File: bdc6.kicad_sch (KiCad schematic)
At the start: 0 parts

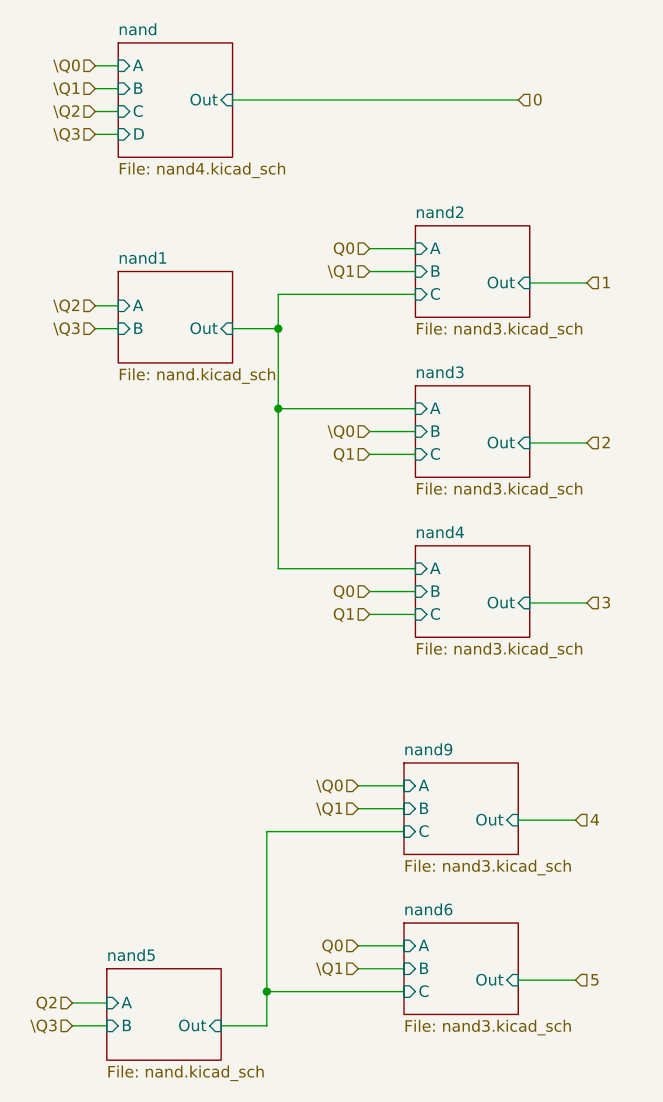
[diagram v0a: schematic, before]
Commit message: corrected output/input type of pins
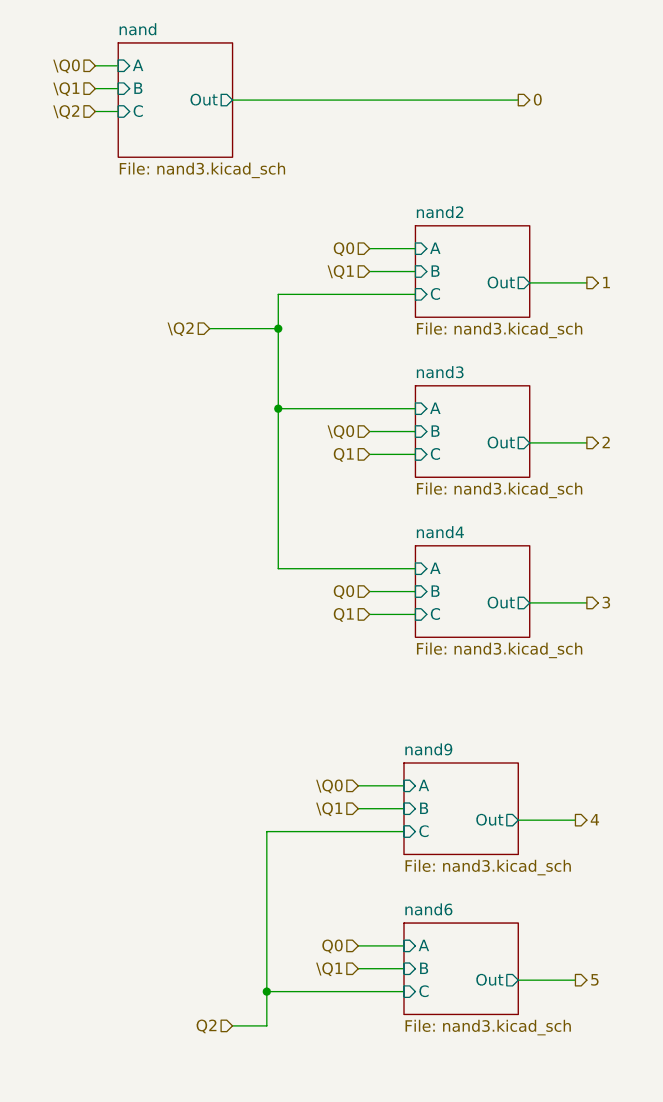
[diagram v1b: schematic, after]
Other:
- removed sheet nand1
- removed sheet nand5
- sheet nand: file nand4.kicad_sch -> nand3.kicad_sch
- sheet nand ports: added none; removed D

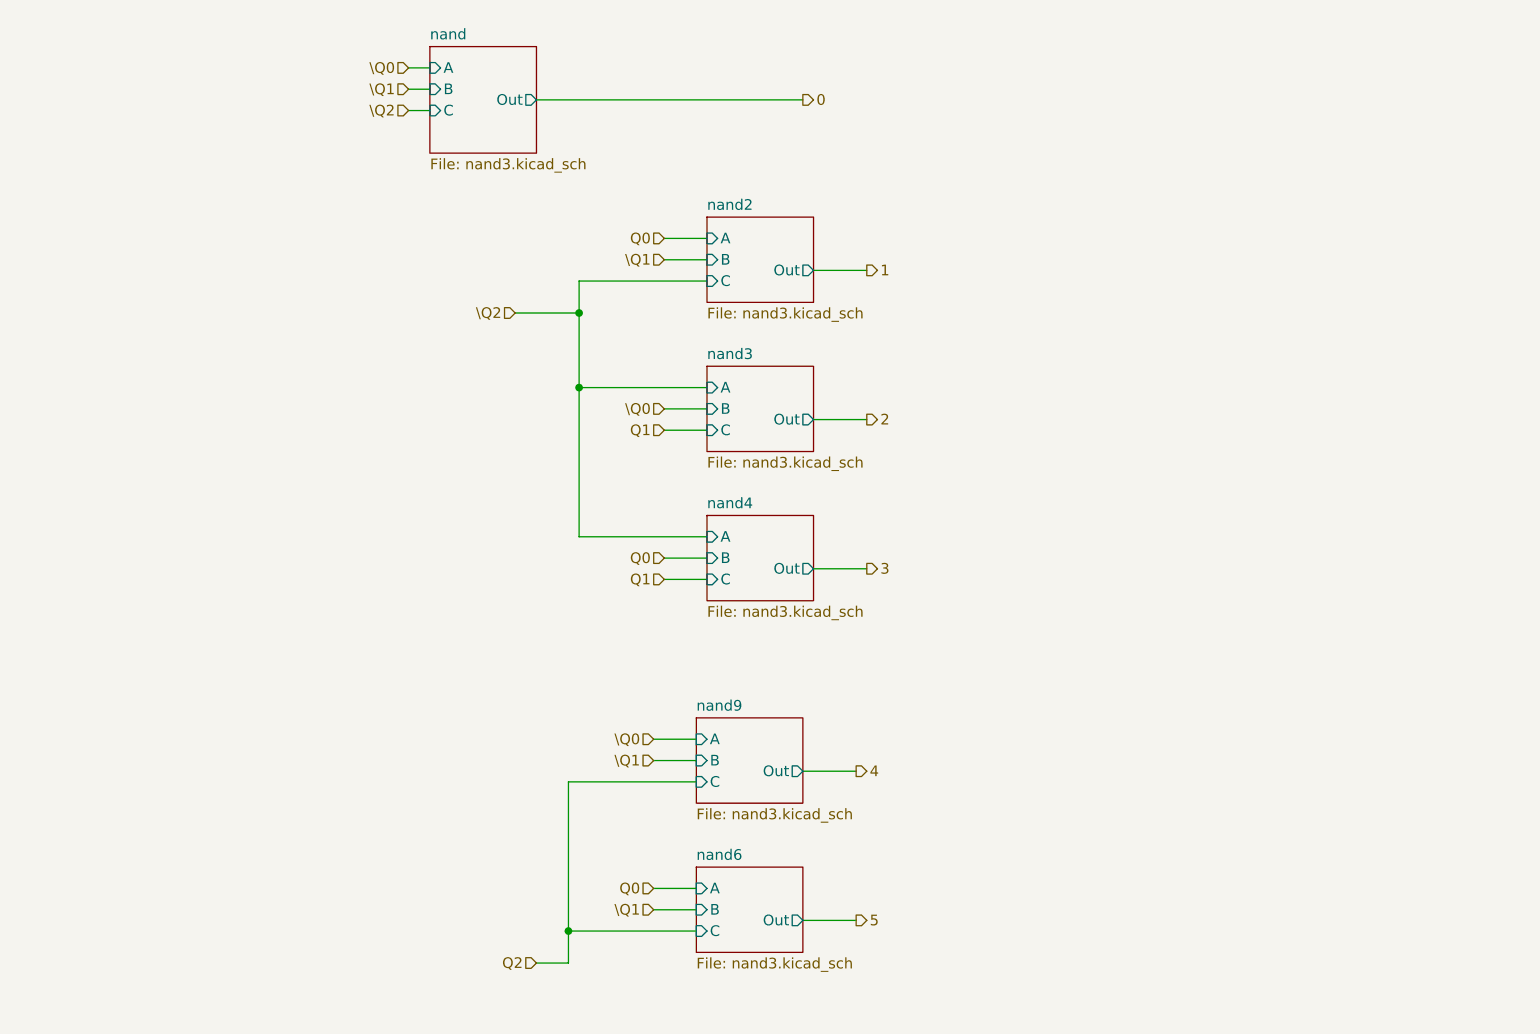
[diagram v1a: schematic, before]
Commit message: replace bcd logic with bin-to-dec module
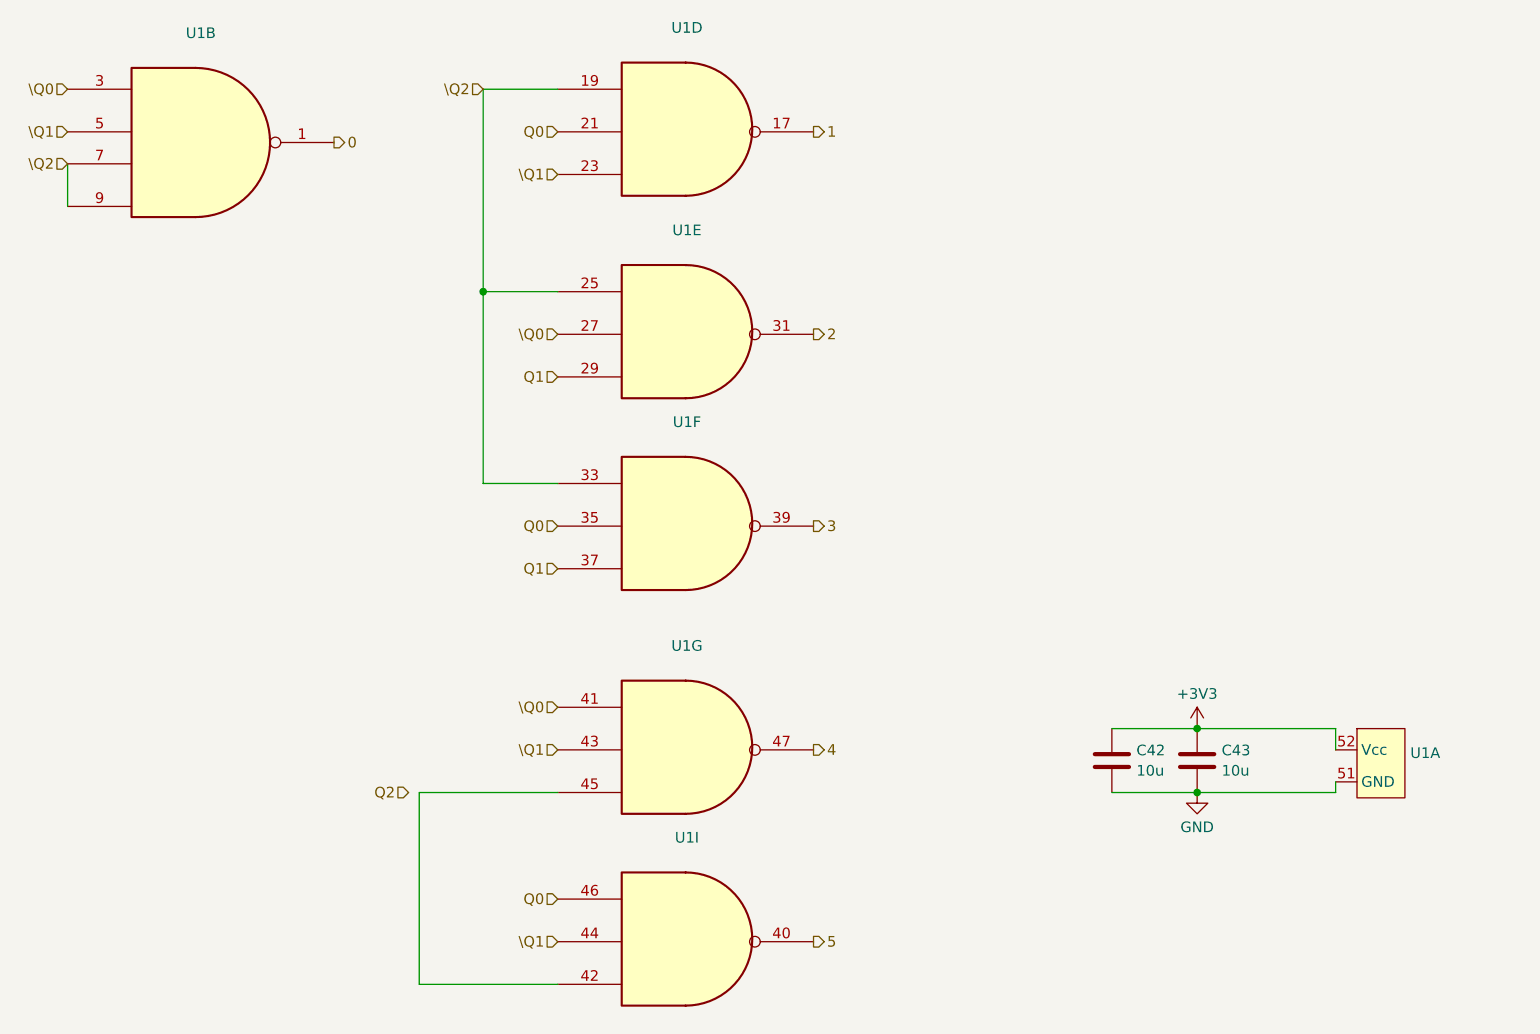
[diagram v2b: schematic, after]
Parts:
- added C42, C43: 10u, Capacitor_SMD:C_0603_1608Metric, symbol Device:C
- added U1: ~, symbol custom:BDC_nands
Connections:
- net 0: now also U1.1
- net 1: now also U1.17
- net 2: now also U1.31
- net 3: now also U1.39
- net 4: now also U1.47
- net 5: now also U1.40
- net Q0: now also U1.21, U1.35, U1.46
- net Q1: now also U1.29, U1.37
- net \Q0: now also U1.27, U1.3, U1.41
- net \Q1: now also U1.23, U1.43, U1.44, U1.5
- net \Q2: now also U1.19, U1.25, U1.33, U1.7, U1.9
- new net: U1.42, U1.45
- new net +3V3: C42.1, C43.1, U1.52 (Vcc)
- new net GND: C42.2, C43.2, U1.51 (GND)
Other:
- removed sheet nand
- removed sheet nand2
- removed sheet nand3
- removed sheet nand4
- removed sheet nand6
- removed sheet nand9

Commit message: added LCSC part numbers
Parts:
- C42, C43: LCSC Part # (none) -> C57112
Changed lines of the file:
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@@
+			)
+		)
+		(property "LCSC Part #" "C57112"
+			(at 165.1 110.49 0)
+			(effects
+				(font
+					(size 1.27 1.27)
+				)
+				(hide yes)
 			)
 		)
@@
 			)
 		)
+		(property "LCSC Part #" ""
+			(at 88.9 26.67 0)
+			(effects
+				(font
+					(size 1.27 1.27)
+				)
+				(hide yes)
+			)
+		)
 		(pin "8"
 		)
@@
 			)
 		)
+		(property "LCSC Part #" "C57112"
+			(at 154.94 110.49 0)
+			(effects
+				(font
+					(size 1.27 1.27)
+				)
+				(hide yes)
+			)
+		)
 		(pin "2"
 		)
@@
 			)
 		)
+		(property "LCSC Part #" ""
+			(at 87.63 123.19 0)
+			(effects
+				(font
+					(size 1.27 1.27)
+				)
+				(hide yes)
+			)
+		)
 		(pin "8"
 		)
@@
 			)
 		)
+		(property "LCSC Part #" ""
+			(at 177.8 110.49 0)
+			(effects
+				(font
+					(size 1.27 1.27)
+				)
+				(hide yes)
+			)
+		)
 		(pin "8"
 		)
@@
 			)
 		)
+		(property "LCSC Part #" ""
+			(at 87.63 50.8 0)
+			(effects
+				(font
+					(size 1.27 1.27)
+				)
+				(hide yes)
+			)
+		)
 		(pin "8"
 		)
@@
 			)
 		)
+		(property "LCSC Part #" ""
+			(at 88.9 100.33 0)
+			(effects
+				(font
+					(size 1.27 1.27)
+				)
+				(hide yes)
+			)
+		)
 		(pin "8"
 		)
@@
 			)
 		)
+		(property "LCSC Part #" ""
+			(at 36.83 27.94 0)
+			(effects
+				(font
+					(size 1.27 1.27)
+				)
+				(hide yes)
+			)
+		)
 		(pin "8"
 		)
@@
 			(at 87.63 73.66 0)
 			(effects
+				(font
+					(size 1.27 1.27)
+				)
+				(hide yes)
+			)
+		)
+		(property "LCSC Part #" ""
+			(at 87.63 73.66 0)
+			(effects

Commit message: switched clock to bjt astable multivibrator
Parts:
- U1: now not fitted
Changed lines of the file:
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@@
 		(in_bom yes)
 		(on_board yes)
-		(dnp no)
+		(dnp yes)
 		(fields_autoplaced yes)
 		(property "Reference" "U1"
@@
 		(in_bom yes)
 		(on_board yes)
-		(dnp no)
+		(dnp yes)
 		(fields_autoplaced yes)
 		(property "Reference" "U1"
@@
 		(in_bom yes)
 		(on_board yes)
-		(dnp no)
+		(dnp yes)
 		(fields_autoplaced yes)
 		(property "Reference" "U1"
@@
 		(in_bom yes)
 		(on_board yes)
-		(dnp no)
+		(dnp yes)
 		(fields_autoplaced yes)
 		(property "Reference" "U1"
@@
 		(in_bom yes)
 		(on_board yes)
-		(dnp no)
+		(dnp yes)
 		(fields_autoplaced yes)
 		(property "Reference" "U1"
@@
 		(in_bom yes)
 		(on_board yes)
-		(dnp no)
+		(dnp yes)
 		(fields_autoplaced yes)
 		(property "Reference" "U1"
@@
 		(in_bom yes)
 		(on_board yes)
-		(dnp no)
+		(dnp yes)
 		(fields_autoplaced yes)
 		(property "Reference" "U1"

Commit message: changed some components to lcsc parts
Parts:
- U1: now fitted
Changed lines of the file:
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@@
 			)
 		)
-		(property "Datasheet" "~"
+		(property "Datasheet" "https://www.lcsc.com/datasheet/lcsc_datasheet_2408090958_MDD-Microdiode-Semiconductor-S3MF_C64874.pdf"
 			(at 165.1 110.49 0)
 			(effects
@@
 		(in_bom yes)
 		(on_board yes)
-		(dnp yes)
+		(dnp no)
 		(fields_autoplaced yes)
 		(property "Reference" "U1"
@@
 			)
 		)
-		(property "Datasheet" "~"
+		(property "Datasheet" "https://www.lcsc.com/datasheet/lcsc_datasheet_2408090958_MDD-Microdiode-Semiconductor-S3MF_C64874.pdf"
 			(at 154.94 110.49 0)
 			(effects
@@
 		(in_bom yes)
 		(on_board yes)
-		(dnp yes)
+		(dnp no)
 		(fields_autoplaced yes)
 		(property "Reference" "U1"
@@
 		(in_bom yes)
 		(on_board yes)
-		(dnp yes)
+		(dnp no)
 		(fields_autoplaced yes)
 		(property "Reference" "U1"
@@
 		(in_bom yes)
 		(on_board yes)
-		(dnp yes)
+		(dnp no)
 		(fields_autoplaced yes)
 		(property "Reference" "U1"
@@
 		(in_bom yes)
 		(on_board yes)
-		(dnp yes)
+		(dnp no)
 		(fields_autoplaced yes)
 		(property "Reference" "U1"
@@
 		(in_bom yes)
 		(on_board yes)
-		(dnp yes)
+		(dnp no)
 		(fields_autoplaced yes)
 		(property "Reference" "U1"
@@
 		(in_bom yes)
 		(on_board yes)
-		(dnp yes)
+		(dnp no)
 		(fields_autoplaced yes)
 		(property "Reference" "U1"
